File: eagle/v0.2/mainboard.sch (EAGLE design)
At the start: 40 parts, among them IC1 74HCT151D, IC2 74HCT151D, IC3 74HCT151D, IC4 74HCT151D, IC5 74HCT151D, IC6 74HCT151D, IC7 74HC590D, IC8 74HC02D, J1 12401832E402A, J2 12401832E402A, J3 12401832E402A, J4 12401832E402A, J5 12401832E402A, J7 L77HDE15SD1CH4RHNVGA

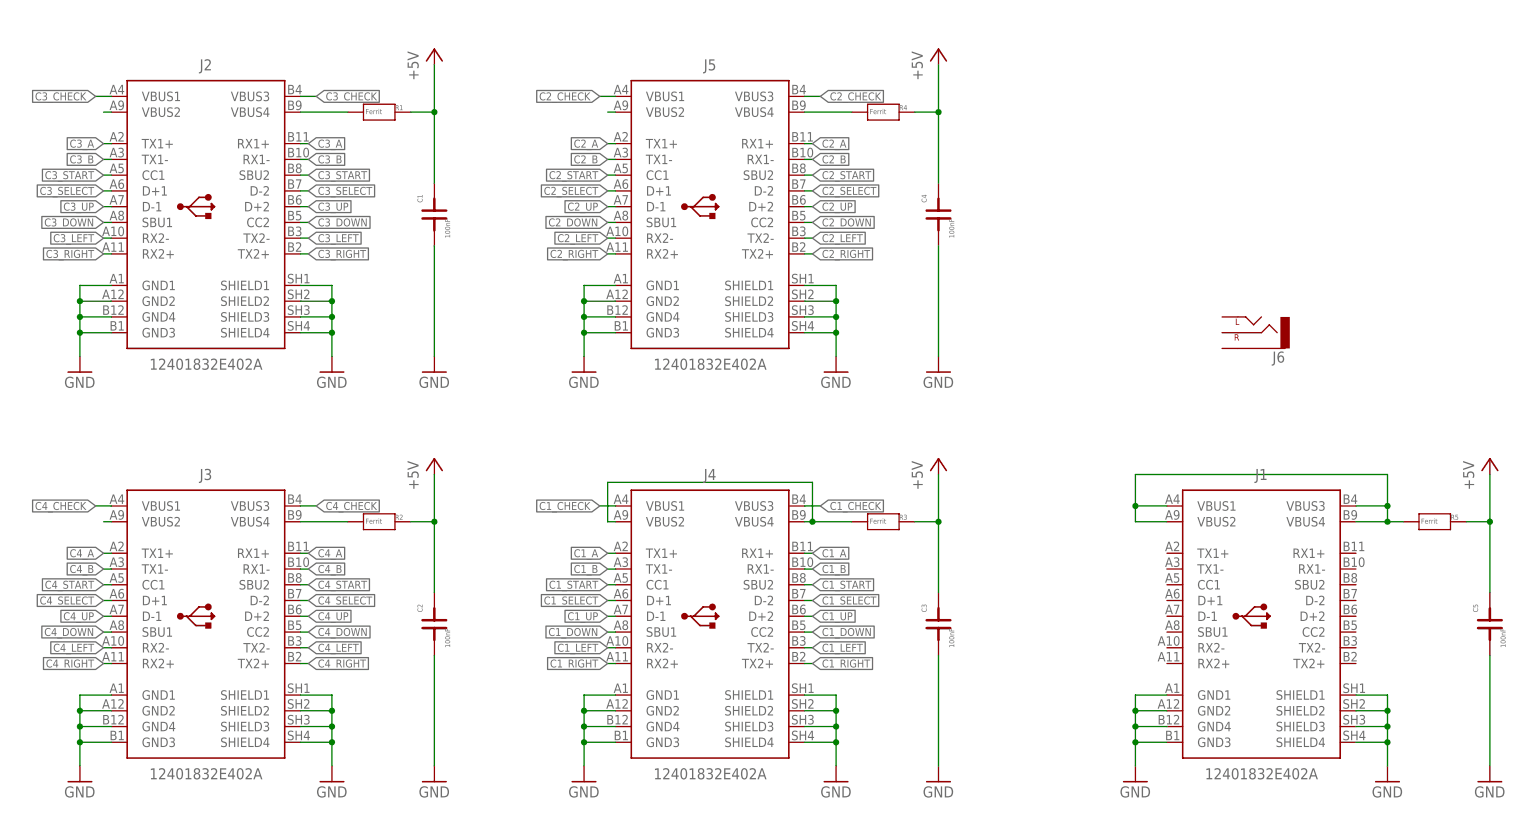
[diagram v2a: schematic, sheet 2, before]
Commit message: replaced usb-c 24 pin reciver with 12 pin reciver
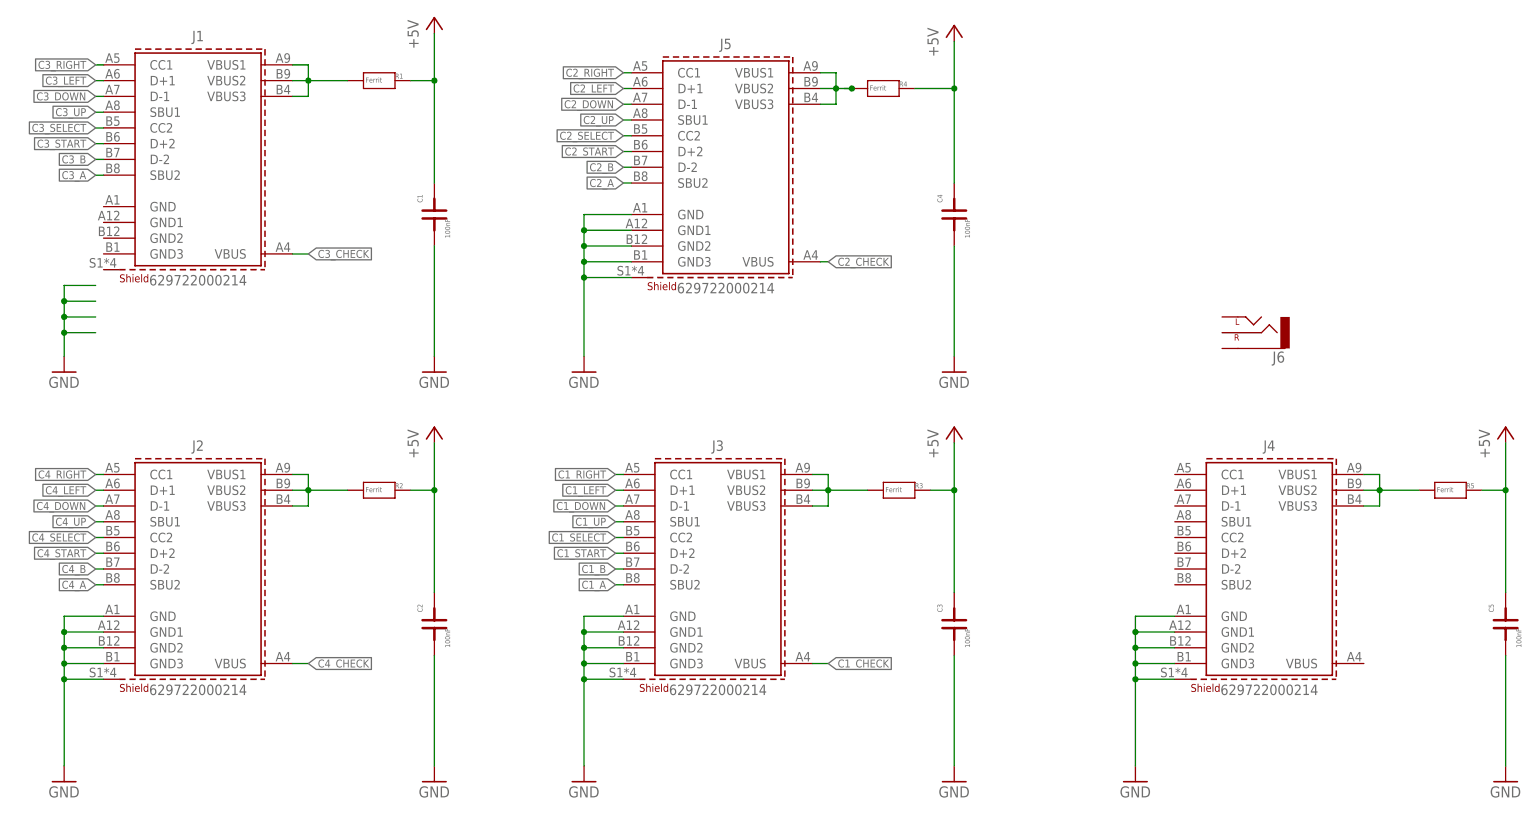
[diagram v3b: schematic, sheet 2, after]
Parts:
- J1, J2, J3, J4, J5: value 12401832E402A -> 629722000214; device Connector_USB:12401832E402A -> Eagle_WR-USB (rev22c):629722000214_CUSTOM
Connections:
- removed net N$21: J3.VBUS2
- removed net N$23: J4.VBUS2, J4.VBUS4, R3.1
- removed net N$28: J5.VBUS2
- removed net N$3: J1.VBUS1, J1.VBUS2, J1.VBUS3, J1.VBUS4, R5.1
- removed net SHIELD4: J1.SHIELD1, J1.SHIELD2, J1.SHIELD3, J1.SHIELD4, J2.SHIELD1, J2.SHIELD2, J2.SHIELD3, J2.SHIELD4, J3.SHIELD1, J3.SHIELD2, J3.SHIELD3, J3.SHIELD4, J4.SHIELD1, J4.SHIELD2, J4.SHIELD3, J4.SHIELD4, J5.SHIELD1, J5.SHIELD2, J5.SHIELD3, J5.SHIELD4
- new net N$2: J2.VBUS1, J2.VBUS2, J2.VBUS3, R2.1
- net C1_A: now also J3.SBU2; no longer J4.RX1+, J4.TX1+
- net C1_B: now also J3.D-2; no longer J4.RX1-, J4.TX1-
- net C1_CHECK: now also J3.VBUS; no longer J4.VBUS1, J4.VBUS3
- net C1_DOWN: now also J3.D-1; no longer J4.CC2, J4.SBU1
- net C1_LEFT: now also J3.D+1; no longer J4.RX2-, J4.TX2-
- net C1_RIGHT: now also J3.CC1; no longer J4.RX2+, J4.TX2+
- net C1_SELECT: now also J3.CC2; no longer J4.D+1, J4.D-2
- net C1_START: now also J3.D+2; no longer J4.CC1, J4.SBU2
- net C1_UP: now also J3.SBU1; no longer J4.D+2, J4.D-1
- net C2_A: now also J5.SBU2; no longer J5.RX1+, J5.TX1+
- net C2_B: now also J5.D-2; no longer J5.RX1-, J5.TX1-
- net C2_CHECK: now also J5.VBUS; no longer J5.VBUS1, J5.VBUS3
- net C2_DOWN: now also J5.D-1; no longer J5.CC2, J5.SBU1
- net C2_LEFT: now also J5.D+1; no longer J5.RX2-, J5.TX2-
- net C2_RIGHT: now also J5.CC1; no longer J5.RX2+, J5.TX2+
- net C2_SELECT: now also J5.CC2; no longer J5.D+1, J5.D-2
- net C2_START: now also J5.D+2; no longer J5.CC1, J5.SBU2
- net C2_UP: now also J5.SBU1; no longer J5.D+2, J5.D-1
- net C3_A: now also J1.SBU2; no longer J2.RX1+, J2.TX1+
- net C3_B: now also J1.D-2; no longer J2.RX1-, J2.TX1-
- net C3_CHECK: now also J1.VBUS; no longer J2.VBUS1, J2.VBUS3
- net C3_DOWN: now also J1.D-1; no longer J2.CC2, J2.SBU1
- net C3_LEFT: now also J1.D+1; no longer J2.RX2-, J2.TX2-
- net C3_RIGHT: now also J1.CC1; no longer J2.RX2+, J2.TX2+
- net C3_SELECT: now also J1.CC2; no longer J2.D+1, J2.D-2
- net C3_START: now also J1.D+2; no longer J2.CC1, J2.SBU2
- net C3_UP: now also J1.SBU1; no longer J2.D+2, J2.D-1
- net C4_A: now also J2.SBU2; no longer J3.RX1+, J3.TX1+
- net C4_B: now also J2.D-2; no longer J3.RX1-, J3.TX1-
- net C4_CHECK: now also J2.VBUS; no longer J3.VBUS1, J3.VBUS3
- net C4_DOWN: now also J2.D-1; no longer J3.CC2, J3.SBU1
- net C4_LEFT: now also J2.D+1; no longer J3.RX2-, J3.TX2-
- net C4_RIGHT: now also J2.CC1; no longer J3.RX2+, J3.TX2+
- net C4_SELECT: now also J2.CC2; no longer J3.D+1, J3.D-2
- net C4_START: now also J2.D+2; no longer J3.CC1, J3.SBU2
- net C4_UP: now also J2.SBU1; no longer J3.D+2, J3.D-1
- net GND: now also J2.GND, J2.SHIELD, J3.GND, J3.SHIELD, J4.GND, J4.SHIELD, J5.GND, J5.SHIELD; no longer J1.GND1, J1.GND2, J1.GND3, J1.GND4, J2.GND4, J3.GND4, J4.GND4, J5.GND4
- net N$1: now also J4.VBUS1, J4.VBUS2, J4.VBUS3, R5.1; no longer J2.VBUS4, R1.1
- net N$26: now also J1.VBUS1, J1.VBUS2, J1.VBUS3, R1.1; no longer J2.VBUS2
- net N$4: now also J5.VBUS1, J5.VBUS2, J5.VBUS3, R4.1; no longer J3.VBUS4, R2.1
- net N$5: now also J3.VBUS1, J3.VBUS2, J3.VBUS3, R3.1; no longer J5.VBUS4, R4.1
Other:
- moved on the sheet: C3, C4, C5, R1, R2, R3, R4, R5
